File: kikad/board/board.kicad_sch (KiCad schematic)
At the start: 18 parts, among them J1 Conn_01x10_Socket, J2 Conn_01x10_Socket, J3 Conn_01x06_Socket, J4 Conn_01x02_Socket, J5 Conn_01x02_Socket, Q1 2N3906, Q2 PN2222A, Q3 BC547, Q4 2N3906, U1 TL431LP

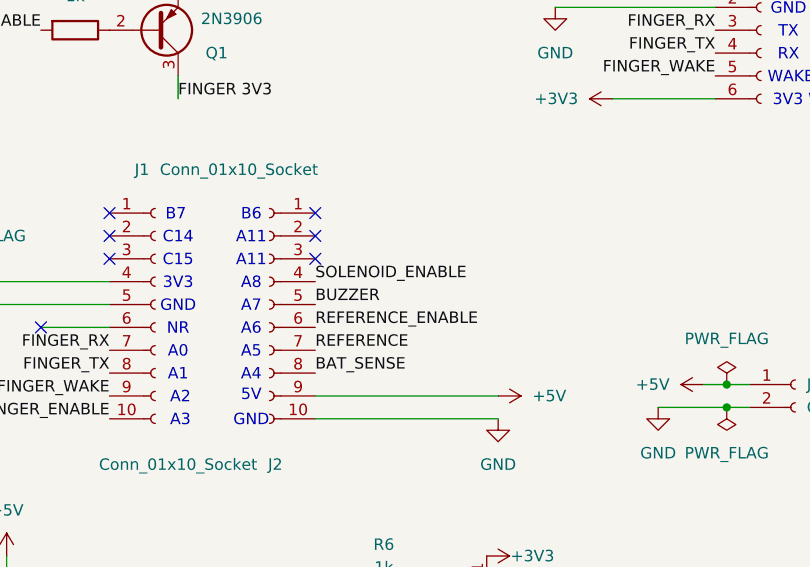
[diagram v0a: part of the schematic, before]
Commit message: add sensor setup
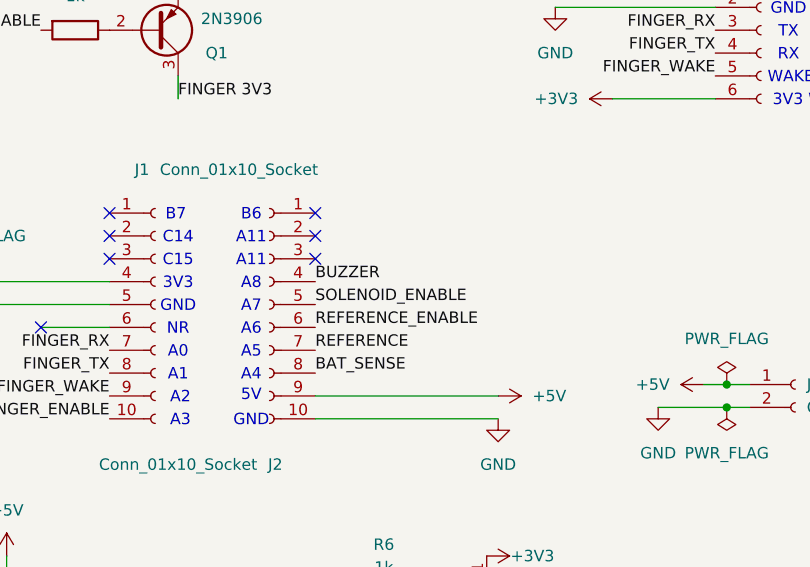
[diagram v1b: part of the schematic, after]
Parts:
- J2: footprint (none) -> Connector_PinSocket_2.54mm:PinSocket_1x10_P2.54mm_Vertical
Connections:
- net BUZZER: now also J2.4 (Pin_4); no longer J2.5 (Pin_5)
- net SOLENOID_ENABLE: now also J2.5 (Pin_5); no longer J2.4 (Pin_4)
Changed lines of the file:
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@@
+		)
+	)
+	(label "SOLENOID_ENABLE"
+		(at 182.88 99.06 0)
+		(effects
+			(font
+				(size 1.27 1.27)
+			)
+			(justify left bottom)
 		)
 	)
@@
 		)
 	)
-	(label "SOLENOID_ENABLE"
+	(label "BUZZER"
 		(at 182.88 96.52 0)
 		(effects
@@
 			)
 			(justify right bottom)
-		)
-	)
-	(label "BUZZER"
-		(at 182.88 99.06 0)
-		(effects
-			(font
-				(size 1.27 1.27)
-			)
-			(justify left bottom)
 		)
 	)
@@
 			)
 		)
-		(property "Footprint" ""
+		(property "Footprint" "Connector_PinSocket_2.54mm:PinSocket_1x10_P2.54mm_Vertical"
 			(at 177.8 99.06 0)
 			(effects
